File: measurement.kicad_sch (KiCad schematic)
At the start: 22 parts, among them U26001 ACS730xLCTR-20AB, U26002 TLV9352

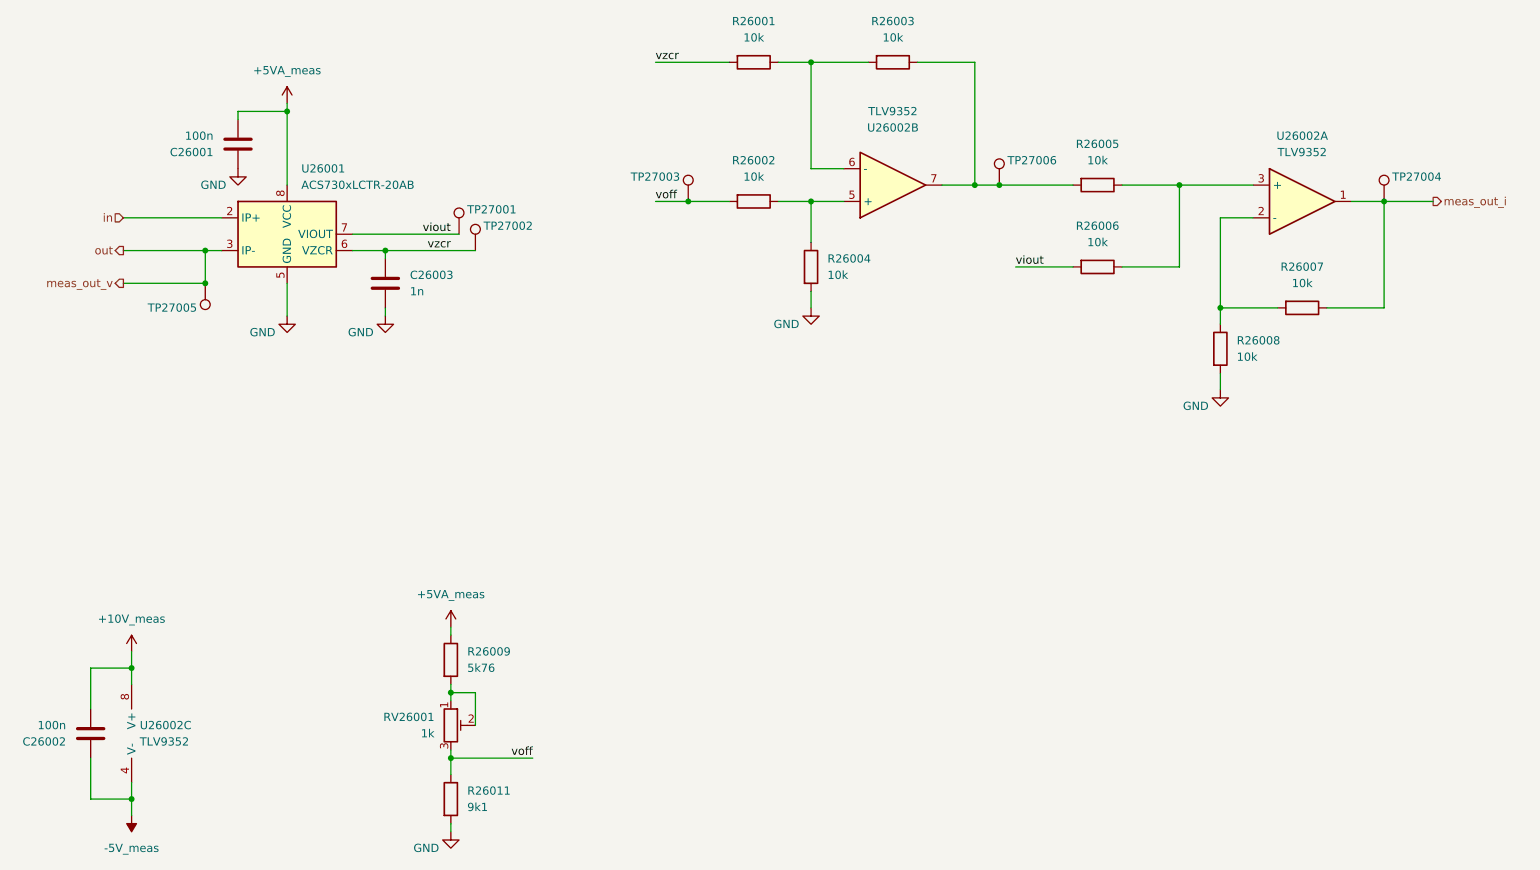
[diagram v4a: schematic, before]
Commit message: edit pss footprint library: export all footprints to library 'pss' and update footprint links
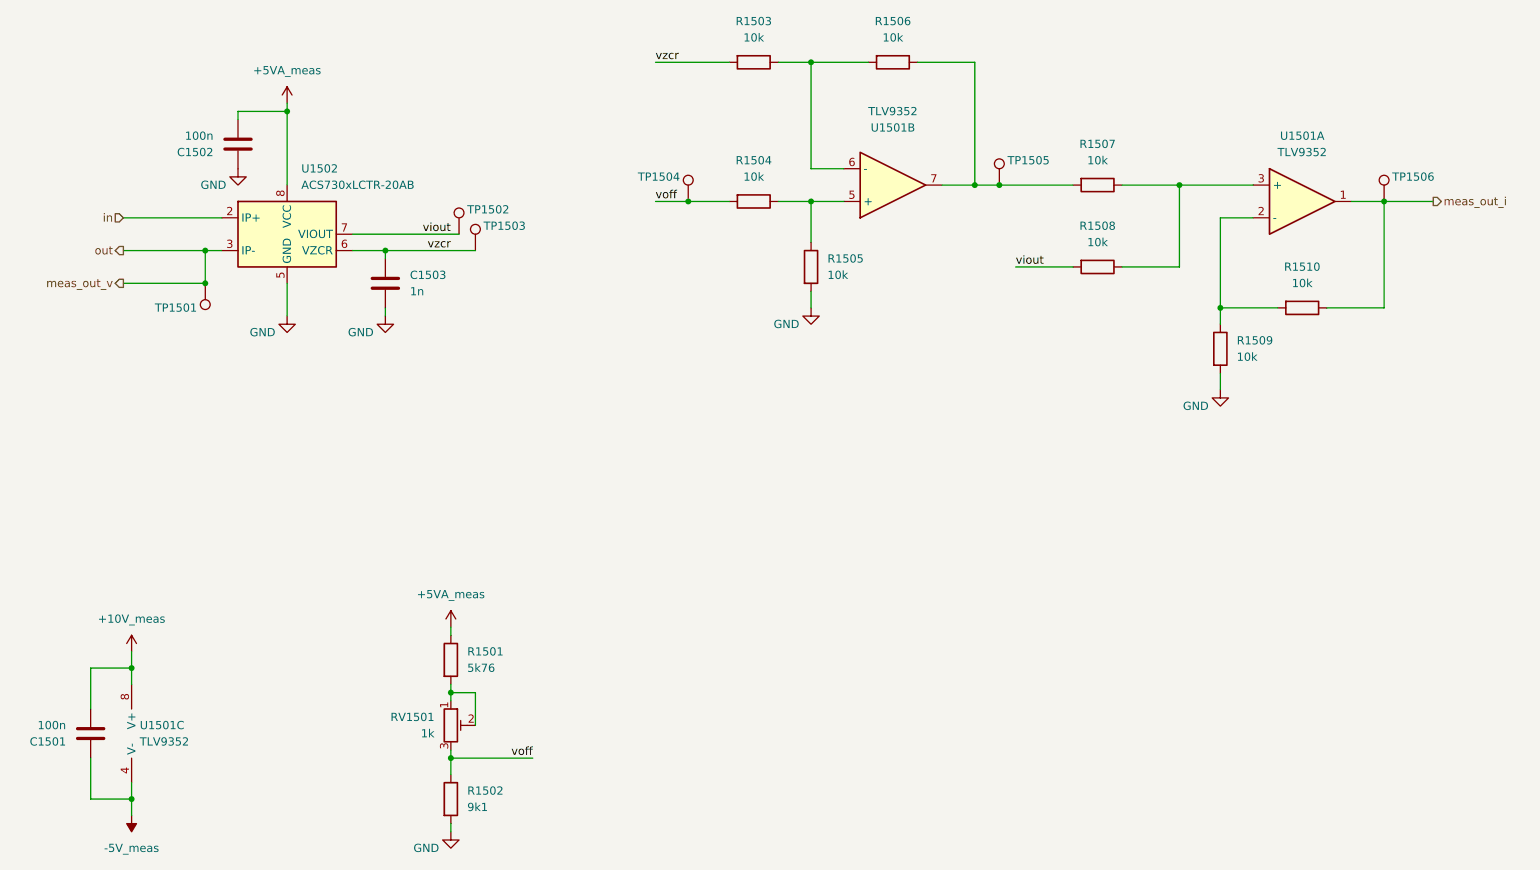
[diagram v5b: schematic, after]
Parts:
- C1501: renamed from C26002; footprint Capacitor_SMD:C_0805_2012Metric_Pad1.18x1.45mm_HandSolder -> pss:C_0805_2012Metric_Pad1.18x1.45mm_HandSolder
- C1502: renamed from C26001; footprint Capacitor_SMD:C_0805_2012Metric_Pad1.18x1.45mm_HandSolder -> pss:C_0805_2012Metric_Pad1.18x1.45mm_HandSolder
- C1503: renamed from C26003; footprint Capacitor_SMD:C_0805_2012Metric_Pad1.18x1.45mm_HandSolder -> pss:C_0805_2012Metric_Pad1.18x1.45mm_HandSolder
- R1501: renamed from R26009; footprint Resistor_SMD:R_1210_3225Metric_Pad1.30x2.65mm_HandSolder -> pss:R_1210_3225Metric_Pad1.30x2.65mm_HandSolder
- R1502: renamed from R26011; footprint Resistor_SMD:R_1210_3225Metric_Pad1.30x2.65mm_HandSolder -> pss:R_1210_3225Metric_Pad1.30x2.65mm_HandSolder
- R1503: renamed from R26001; footprint Resistor_SMD:R_1210_3225Metric_Pad1.30x2.65mm_HandSolder -> pss:R_1210_3225Metric_Pad1.30x2.65mm_HandSolder
- R1504: renamed from R26002; footprint Resistor_SMD:R_1210_3225Metric_Pad1.30x2.65mm_HandSolder -> pss:R_1210_3225Metric_Pad1.30x2.65mm_HandSolder
- R1505: renamed from R26004; footprint Resistor_SMD:R_1210_3225Metric_Pad1.30x2.65mm_HandSolder -> pss:R_1210_3225Metric_Pad1.30x2.65mm_HandSolder
- R1506: renamed from R26003; footprint Resistor_SMD:R_1210_3225Metric_Pad1.30x2.65mm_HandSolder -> pss:R_1210_3225Metric_Pad1.30x2.65mm_HandSolder
- R1507: renamed from R26005; footprint Resistor_SMD:R_1210_3225Metric_Pad1.30x2.65mm_HandSolder -> pss:R_1210_3225Metric_Pad1.30x2.65mm_HandSolder
- R1508: renamed from R26006; footprint Resistor_SMD:R_1210_3225Metric_Pad1.30x2.65mm_HandSolder -> pss:R_1210_3225Metric_Pad1.30x2.65mm_HandSolder
- R1509: renamed from R26008; footprint Resistor_SMD:R_1210_3225Metric_Pad1.30x2.65mm_HandSolder -> pss:R_1210_3225Metric_Pad1.30x2.65mm_HandSolder
- R1510: renamed from R26007; footprint Resistor_SMD:R_1210_3225Metric_Pad1.30x2.65mm_HandSolder -> pss:R_1210_3225Metric_Pad1.30x2.65mm_HandSolder
- U1501: renamed from U26002; footprint Package_SO:SOIC-8_3.9x4.9mm_P1.27mm -> pss:SOIC-8_3.9x4.9mm_P1.27mm
- U1502: renamed from U26001; footprint Package_SO:SOIC-8_3.9x4.9mm_P1.27mm -> pss:SOIC-8_3.9x4.9mm_P1.27mm
- renumbered RV26001 to RV1501, TP27005 to TP1501, TP27001 to TP1502, TP27002 to TP1503, TP27003 to TP1504, TP27006 to TP1505, TP27004 to TP1506
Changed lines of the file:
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@@
 		(on_board yes)
 		(dnp no)
-		(property "Reference" "#PWR026008"
+		(property "Reference" "#PWR01510"
 			(at 220.98 123.19 0)
 			(effects
@@
 		(dnp no)
 		(fields_autoplaced yes)
-		(property "Reference" "#PWR027004"
+		(property "Reference" "#PWR01502"
 			(at 52.07 179.07 0)
 			(effects
@@
 		(dnp no)
 		(fields_autoplaced yes)
-		(property "Reference" "R26009"
+		(property "Reference" "R1501"
 			(at 104.14 157.4799 0)
 			(effects
@@
 			)
 		)
-		(property "Footprint" "Resistor_SMD:R_1210_3225Metric_Pad1.30x2.65mm_HandSolder"
+		(property "Footprint" "pss:R_1210_3225Metric_Pad1.30x2.65mm_HandSolder"
 			(at 99.822 158.75 90)
 			(effects
@@
 		(on_board yes)
 		(dnp no)
-		(property "Reference" "TP27002"
+		(property "Reference" "TP1503"
 			(at 106.68 91.44 0)
 			(effects
@@
 		(on_board yes)
 		(dnp no)
-		(property "Reference" "#PWR026002"
+		(property "Reference" "#PWR01503"
 			(at 68.58 88.9 0)
 			(effects
@@
 		(on_board yes)
 		(dnp no)
-		(property "Reference" "C26003"
+		(property "Reference" "C1503"
 			(at 95.25 99.0599 0)
 			(effects
@@
 			)
 		)
-		(property "Footprint" "Capacitor_SMD:C_0805_2012Metric_Pad1.18x1.45mm_HandSolder"
+		(property "Footprint" "pss:C_0805_2012Metric_Pad1.18x1.45mm_HandSolder"
 			(at 92.4052 104.14 0)
 			(effects
@@
 		(on_board yes)
 		(dnp no)
-		(property "Reference" "TP27004"
+		(property "Reference" "TP1506"
 			(at 247.65 83.82 0)
 			(effects
@@
 		(on_board yes)
 		(dnp no)
-		(property "Reference" "C26001"
+		(property "Reference" "C1502"
 			(at 64.77 80.0101 0)
 			(effects
@@
 			)
 		)
-		(property "Footprint" "Capacitor_SMD:C_0805_2012Metric_Pad1.18x1.45mm_HandSolder"
+		(property "Footprint" "pss:C_0805_2012Metric_Pad1.18x1.45mm_HandSolder"
 			(at 67.6148 74.93 0)
 			(effects
@@
 		(on_board yes)
 		(dnp no)
-		(property "Reference" "TP27006"
+		(property "Reference" "TP1505"
 			(at 187.96 81.28 0)
 			(effects
@@
 		(dnp no)
 		(fields_autoplaced yes)
-		(property "Reference" "R26003"
+		(property "Reference" "R1506"
 			(at 170.18 59.69 90)
 			(effects
@@
 			)
 		)
-		(property "Footprint" "Resistor_SMD:R_1210_3225Metric_Pad1.30x2.65mm_HandSolder"
+		(property "Footprint" "pss:R_1210_3225Metric_Pad1.30x2.65mm_HandSolder"
 			(at 170.18 64.262 90)
 			(effects
@@
 		(dnp no)
 		(fields_autoplaced yes)
-		(property "Reference" "R26005"
+		(property "Reference" "R1507"
 			(at 201.93 78.74 90)
 			(effects
@@
 			)
 		)
-		(property "Footprint" "Resistor_SMD:R_1210_3225Metric_Pad1.30x2.65mm_HandSolder"
+		(property "Footprint" "pss:R_1210_3225Metric_Pad1.30x2.65mm_HandSolder"
 			(at 201.93 83.312 90)
 			(effects
@@
 		(dnp no)
 		(fields_autoplaced yes)
-		(property "Reference" "R26006"
+		(property "Reference" "R1508"
 			(at 201.93 91.44 90)
 			(effects
@@
 			)
 		)
-		(property "Footprint" "Resistor_SMD:R_1210_3225Metric_Pad1.30x2.65mm_HandSolder"
+		(property "Footprint" "pss:R_1210_3225Metric_Pad1.30x2.65mm_HandSolder"
 			(at 201.93 96.012 90)
 			(effects
@@
 		(dnp no)
 		(fields_autoplaced yes)
-		(property "Reference" "#PWR027007"
+		(property "Reference" "#PWR01501"
 			(at 52.07 161.29 0)
 			(effects
@@
 		(dnp no)
 		(fields_autoplaced yes)
-		(property "Reference" "U26001"
+		(property "Reference" "U1502"
 			(at 78.3941 82.55 0)
 			(effects
@@
 			)
 		)
-		(property "Footprint" "Package_SO:SOIC-8_3.9x4.9mm_P1.27mm"
+		(property "Footprint" "pss:SOIC-8_3.9x4.9mm_P1.27mm"
 			(at 85.09 95.25 0)
 			(effects
@@
 		(dnp no)
 		(fields_autoplaced yes)
-		(property "Reference" "R26004"
+		(property "Reference" "R1505"
 			(at 160.02 96.5199 0)
 			(effects
@@
 			)
 		)
-		(property "Footprint" "Resistor_SMD:R_1210_3225Metric_Pad1.30x2.65mm_HandSolder"
+		(property "Footprint" "pss:R_1210_3225Metric_Pad1.30x2.65mm_HandSolder"
 			(at 155.702 97.79 90)
 			(effects
@@
 		(on_board yes)
 		(dnp no)
-		(property "Reference" "C26002"
+		(property "Reference" "C1501"
 			(at 41.91 171.4501 0)
 			(effects
@@
 			)
 		)
-		(property "Footprint" "Capacitor_SMD:C_0805_2012Metric_Pad1.18x1.45mm_HandSolder"
+		(property "Footprint" "pss:C_0805_2012Metric_Pad1.18x1.45mm_HandSolder"
 			(at 44.7548 166.37 0)
 			(effects
@@
 		(dnp no)
 		(fields_autoplaced yes)
-		(property "Reference" "R26007"
+		(property "Reference" "R1510"
 			(at 233.68 97.79 90)
 			(effects
@@
 			)
 		)
-		(property "Footprint" "Resistor_SMD:R_1210_3225Metric_Pad1.30x2.65mm_HandSolder"
+		(property "Footprint" "pss:R_1210_3225Metric_Pad1.30x2.65mm_HandSolder"
 			(at 233.68 102.362 90)
 			(effects
@@
 		(dnp no)
 		(fields_autoplaced yes)
-		(property "Reference" "U26002"
+		(property "Reference" "U1501"
 			(at 233.68 77.47 0)
 			(effects
@@
 			)
 		)
-		(property "Footprint" "Package_SO:SOIC-8_3.9x4.9mm_P1.27mm"
+		(property "Footprint" "pss:SOIC-8_3.9x4.9mm_P1.27mm"
 			(at 233.68 87.63 0)
 			(effects
@@
 		(dnp no)
 		(fields_autoplaced yes)
-		(property "Reference" "R26008"
+		(property "Reference" "R1509"
 			(at 223.52 109.2199 0)
 			(effects
@@
 			)
 		)
-		(property "Footprint" "Resistor_SMD:R_1210_3225Metric_Pad1.30x2.65mm_HandSolder"
+		(property "Footprint" "pss:R_1210_3225Metric_Pad1.30x2.65mm_HandSolder"
 			(at 219.202 110.49 90)
 			(effects
@@
 		(on_board yes)
 		(dnp no)
-		(property "Reference" "TP27003"
+		(property "Reference" "TP1504"
 			(at 137.16 83.82 0)
 			(effects
@@
 		(on_board yes)
 		(dnp no)
-		(property "Reference" "TP27005"
+		(property "Reference" "TP1501"
 			(at 62.23 104.14 0)
 			(effects
@@
 		(dnp no)
 		(fields_autoplaced yes)
-		(property "Reference" "#PWR027009"
+		(property "Reference" "#PWR01507"
 			(at 101.6 157.48 0)
 			(effects
@@
 		(dnp no)
 		(fields_autoplaced yes)
-		(property "Reference" "R26011"
+		(property "Reference" "R1502"
 			(at 104.14 179.0699 0)
 			(effects
@@
 			)
 		)
-		(property "Footprint" "Resistor_SMD:R_1210_3225Metric_Pad1.30x2.65mm_HandSolder"
+		(property "Footprint" "pss:R_1210_3225Metric_Pad1.30x2.65mm_HandSolder"
 			(at 99.822 180.34 90)
 			(effects
@@
 		(dnp no)
 		(fields_autoplaced yes)
-		(property "Reference" "R26001"
+		(property "Reference" "R1503"
 			(at 148.59 59.69 90)
 			(effects
@@
 			)
 		)
-		(property "Footprint" "Resistor_SMD:R_1210_3225Metric_Pad1.30x2.65mm_HandSolder"
+		(property "Footprint" "pss:R_1210_3225Metric_Pad1.30x2.65mm_HandSolder"
 			(at 148.59 64.262 90)
 			(effects
@@
 		(dnp no)
 		(fields_autoplaced yes)
-		(property "Reference" "RV26001"
+		(property "Reference" "RV1501"
 			(at 99.06 167.6399 0)
 			(effects
@@
 		(on_board yes)
 		(dnp no)
-		(property "Reference" "#PWR026003"
+		(property "Reference" "#PWR01505"
 			(at 76.2 111.76 0)
 			(effects
@@
 		(dnp no)
 		(fields_autoplaced yes)
-		(property "Reference" "U26002"
+		(property "Reference" "U1501"
 			(at 53.34 168.9099 0)
 			(effects
@@
 			)
 		)
-		(property "Footprint" "Package_SO:SOIC-8_3.9x4.9mm_P1.27mm"
+		(property "Footprint" "pss:SOIC-8_3.9x4.9mm_P1.27mm"
 			(at 54.61 170.18 0)
 			(effects
@@
 		(on_board yes)
 		(dnp no)
-		(property "Reference" "#PWR026010"
+		(property "Reference" "#PWR01508"
 			(at 101.6 191.77 0)
 			(effects
@@
 		(on_board yes)
 		(dnp no)
-		(property "Reference" "#PWR026004"
+		(property "Reference" "#PWR01506"
 			(at 91.44 111.76 0)
 			(effects
@@
 		(on_board yes)
 		(dnp no)
-		(property "Reference" "TP27001"
+		(property "Reference" "TP1502"
 			(at 104.14 88.9 0)
 			(effects
@@
 		(on_board yes)
 		(dnp no)
-		(property "Reference" "#PWR026007"
+		(property "Reference" "#PWR01509"
 			(at 157.48 110.49 0)
 			(effects
@@
 		(dnp no)
 		(fields_autoplaced yes)
-		(property "Reference" "R26002"
+		(property "Reference" "R1504"
 			(at 148.59 81.28 90)
 			(effects
@@
 			)
 		)
-		(property "Footprint" "Resistor_SMD:R_1210_3225Metric_Pad1.30x2.65mm_HandSolder"
+		(property "Footprint" "pss:R_1210_3225Metric_Pad1.30x2.65mm_HandSolder"
 			(at 148.59 85.852 90)
 			(effects
@@
 		(dnp no)
 		(fields_autoplaced yes)
-		(property "Reference" "#PWR027010"
+		(property "Reference" "#PWR01504"
 			(at 76.2 76.2 0)
 			(effects
@@
 		(on_board yes)
 		(dnp no)
-		(property "Reference" "U26002"
+		(property "Reference" "U1501"
 			(at 170.18 76.2 0)
 			(effects
@@
 			)
 		)
-		(property "Footprint" "Package_SO:SOIC-8_3.9x4.9mm_P1.27mm"
+		(property "Footprint" "pss:SOIC-8_3.9x4.9mm_P1.27mm"
 			(at 170.18 85.09 0)
 			(effects
